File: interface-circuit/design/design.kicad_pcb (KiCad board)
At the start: 2 copper layers, 23 parts, among them J10 Screw_Terminal_01x02, J11 Conn_01x02_Male, J12 Conn_01x02_Male, J2 Screw_Terminal_01x05, J3 Screw_Terminal_01x05, J4 Screw_Terminal_01x02, J5 Conn_01x02_Male, J6 Conn_01x02_Male, J7 Conn_01x03_Male, J8 Conn_01x03_Male, J9 Screw_Terminal_01x02, Q1 2N3904-AP, Q2 2N3904-AP, Q3 2N3904-AP, U1 LogicLevelConverter_BOB-08745

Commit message: WIP
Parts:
- U1: footprint custom-footprints:LOGIC_LEVEL_CONVERTER_BOB11978_BOB8745_XC4486 -> custom-footprints:LOGIC_LEVEL_CONVERTER_BOB-8745
- moved J4 109.6 mm to (127.0, 151.1), turned to 0 degrees
- moved J12 99.4 mm to (112.0, 128.5), turned to 0 degrees
- moved J6 96.6 mm to (138.4, 108.0)
- moved J10 94.9 mm to (138.4, 85.1), turned to 90 degrees
- moved J2 92.4 mm to (138.4, 127.0), turned to 90 degrees
- moved J5 89.9 mm to (34.3, 127.0), turned to 0 degrees
- moved Q3 81.0 mm to (114.3, 80.0), turned to 270 degrees
- moved A1 80.5 mm to (57.4, 119.4)
- moved J3 77.8 mm to (43.2, 149.9), turned to 0 degrees
- moved J9 75.7 mm to (138.4, 97.8), turned to 90 degrees
- moved D1 69.4 mm to (129.5, 108.0)
- moved Q2 67.1 mm to (114.3, 92.7), turned to 270 degrees
- moved D2 66.3 mm to (129.5, 97.8)
- moved Q1 65.2 mm to (114.3, 102.9)
- moved R2 63.2 mm to (109.2, 105.4)
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
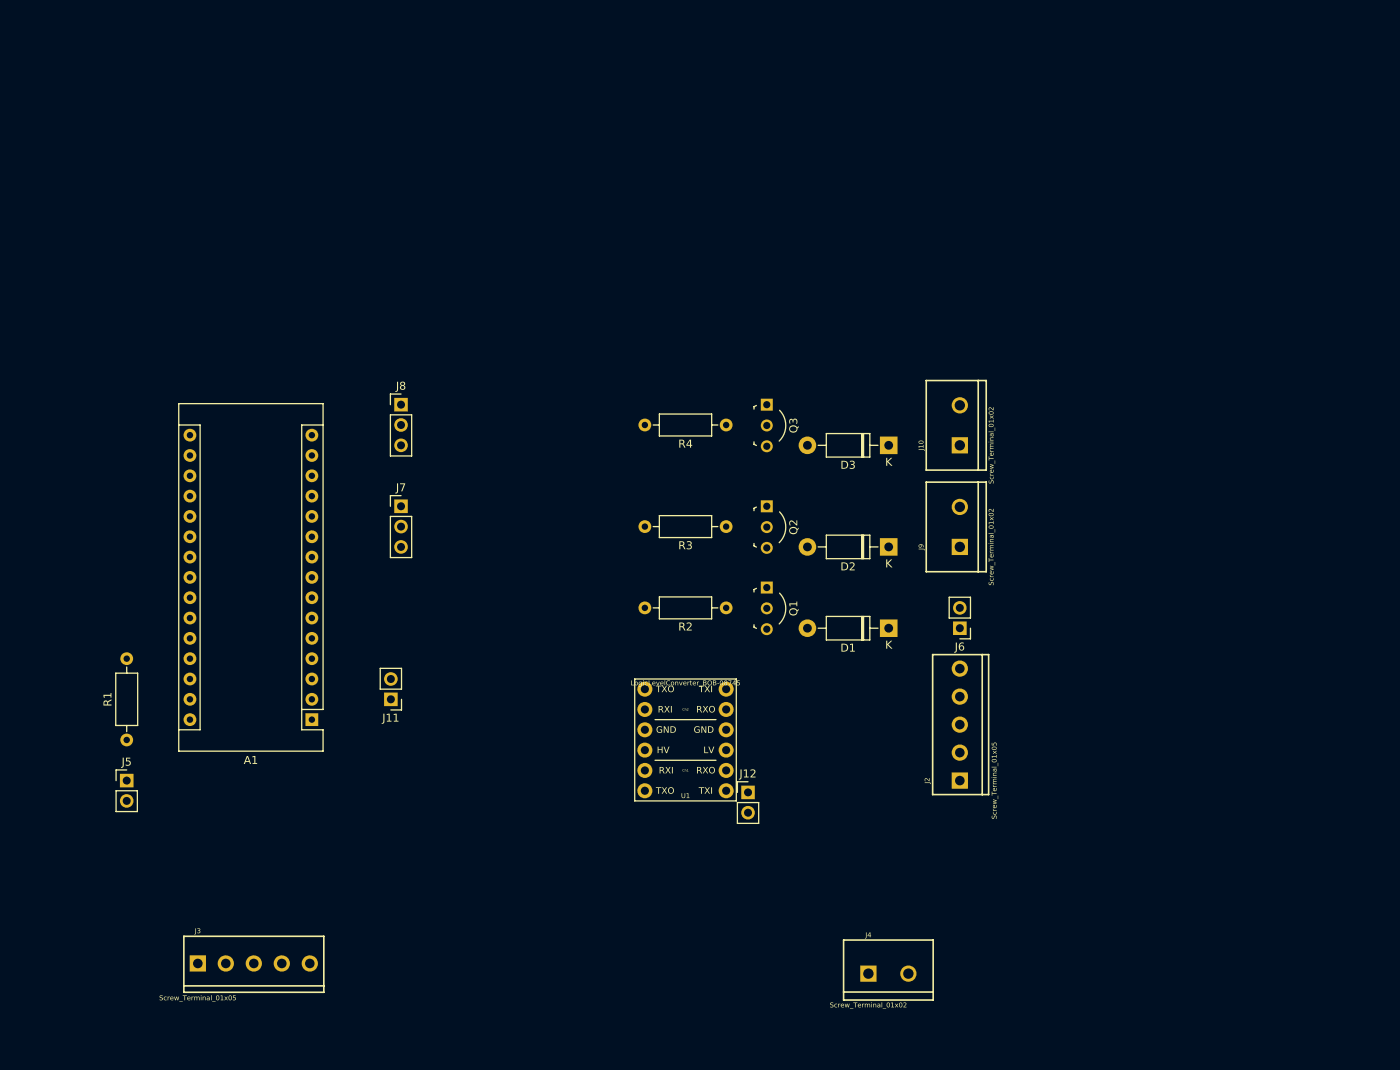
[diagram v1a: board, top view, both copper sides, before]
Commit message: Cannot get the custom component to work, flipped in pcb new and labels associated with wrong sides
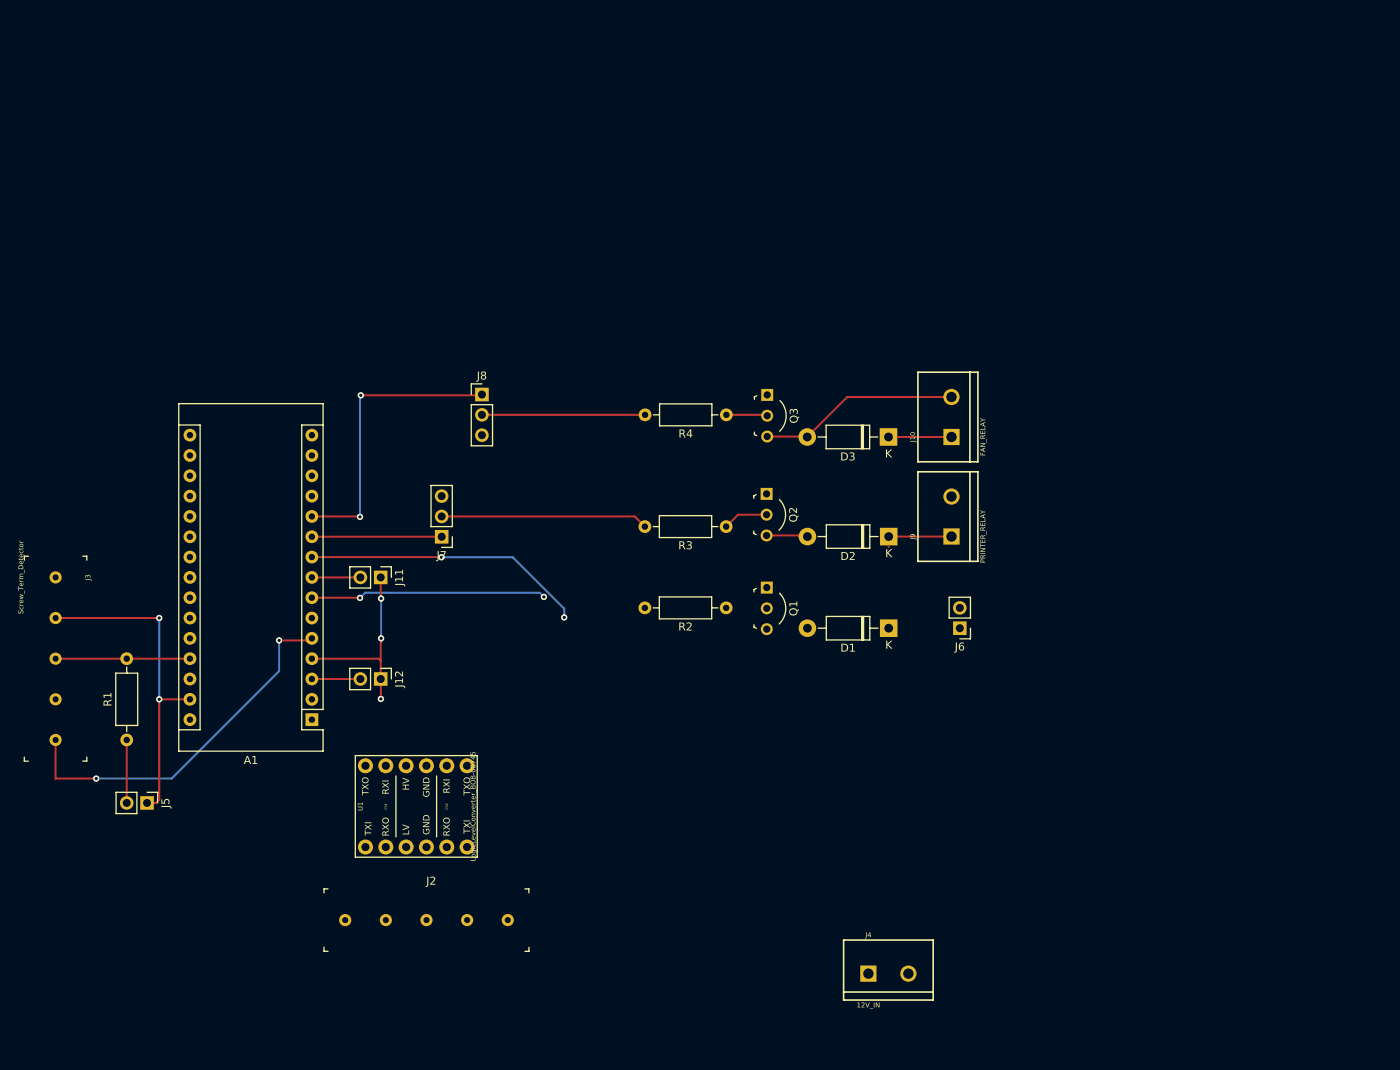
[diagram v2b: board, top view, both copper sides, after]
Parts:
- J10: value Screw_Terminal_01x02 -> FAN_RELAY
- J11: value Conn_01x02_Male -> Conn_Switch
- J12: value Conn_01x02_Male -> Conn_Reset
- J2: value Screw_Terminal_01x05 -> Screw_Term_RPi; footprint Connectors:SCREWTERMINAL-3.5MM-5 -> digikey-footprints:Term_Block_1x5_P5.08mm
- J3: value Screw_Terminal_01x05 -> Screw_Term_Detector; footprint Connectors:SCREWTERMINAL-3.5MM-5 -> digikey-footprints:Term_Block_1x5_P5.08mm
- J4: value Screw_Terminal_01x02 -> 12V_IN
- J5: value Conn_01x02_Male -> Conn_Pwr_LED
- J6: value Conn_01x02_Male -> Conn_Piezo
- J7: value Conn_01x03_Male -> Conn_Printer_Mode
- J8: value Conn_01x03_Male -> Conn_Fan_Mode
- J9: value Screw_Terminal_01x02 -> PRINTER_RELAY
- moved J2 78.8 mm to (61.6, 144.4), turned to 0 degrees
- moved J3 51.4 mm to (25.4, 101.6), turned to 270 degrees
- moved J12 48.1 mm to (66.0, 114.3), turned to 270 degrees
- moved U1 34.7 mm to (70.5, 130.2), turned to 90 degrees
- moved J11 15.3 mm to (66.0, 101.6), turned to 270 degrees
- moved J8 10.2 mm to (78.7, 78.7)
- moved J7 6.35 mm to (73.7, 96.5), turned to 180 degrees
- moved J5 3.78 mm to (36.8, 129.8), turned to 270 degrees
- moved J9 1.66 mm to (137.4, 96.5)
- moved Q2 1.55 mm to (114.3, 91.2)
- moved J10 1.47 mm to (137.4, 84.0)
- moved D2 1.30 mm to (129.5, 96.5)
- moved R4 1.27 mm to (109.2, 81.3)
- moved Q3 1.22 mm to (114.4, 78.8)
- moved D3 1.04 mm to (129.5, 84.0)
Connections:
- A1 pad 29: Net-(A1-Pad29) -> GND
- J2 pad 1: /LV_FanPowerDemand -> /LV_PrinterPowerStatus
- J2 pad 4: /LV_AlarmTriggered -> /LV_FanPowerDemand
- J2 pad 5: /LV_PrinterPowerStatus -> /LV_AlarmTriggered
- U1 pad 1: /HV_PrinterPowerStatus -> /LV_FanPowerDemand
- U1 pad 10: /LV_AlarmTriggered -> /HV_FanPowerDemand
- U1 pad 11: /LV_PrinterPowerDemand -> /LV_PrinterPowerStatus
- U1 pad 12: /LV_FanPowerDemand -> /LV_AlarmTriggered
- U1 pad 2: /HV_AlarmTriggered -> /LV_FanPowerDemand
- U1 pad 3: /HV_PrinterPowerDemand -> /HV_PrinterPowerStatus
- U1 pad 4: /HV_FanPowerDemand -> /HV_AlarmTriggered
- U1 pad 9: /LV_PrinterPowerStatus -> /HV_PrinterPowerDemand
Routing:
- net GND: track 0.00 -> 65.5 mm, vias 0 -> 5
- net /DETECTOR_SIGNAL: track 0.00 -> 46.4 mm, vias 0 -> 2
- net /D8_FAN_RELAY: track 0.00 -> 36.4 mm, vias 0 -> 2
- net /HV_AlarmTriggered: track 0.00 -> 35.3 mm, vias 0 -> 2
- net /HV_FanPowerDemand: track 0.00 -> 29.5 mm, vias 0 -> 2
- net /HV_PrinterPowerStatus: track 0.00 -> 25.9 mm
- net Net-(D3-Pad2): track 0.00 -> 25.1 mm
- net /SW_FAN_RELAY: track 0.00 -> 20.4 mm
- net +5V: track 0.00 -> 16.8 mm
- net /D7_PRINTER_RELAY: track 0.00 -> 16.2 mm
- net +12V: track 0.00 -> 15.8 mm
- net Net-(J5-Pad2): track 0.00 -> 7.87 mm
- net /SOFT_SWITCH: track 0.00 -> 6.06 mm
- net /RESET: track 0.00 -> 6.06 mm
- net Net-(Q2-Pad2): track 0.00 -> 5.67 mm
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
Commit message: Done with manual routing
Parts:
- moved J3 123.5 mm to (146.8, 124.5)
- moved J4 46.4 mm to (147.3, 109.4), turned to 90 degrees
- moved J12 29.0 mm to (43.2, 132.2), turned to 90 degrees
- moved J2 17.6 mm to (73.7, 157.3)
- moved U1 15.2 mm to (82.6, 139.4)
- moved D1 10.3 mm to (139.8, 109.2)
- moved D2 10.2 mm to (139.7, 96.5)
- moved J9 10.2 mm to (147.5, 96.5)
- moved J10 9.94 mm to (147.3, 83.7)
- moved R4 7.98 mm to (116.8, 78.8)
- moved D3 7.65 mm to (137.2, 83.8)
- moved Q3 5.11 mm to (114.3, 83.9), turned to 0 degrees
- moved J7 5.03 mm to (78.7, 96.5), turned to 90 degrees
- moved J6 4.01 mm to (137.2, 104.1), turned to 90 degrees
- moved R3 1.24 mm to (109.2, 94.0)
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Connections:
- J2 pad 1: /LV_PrinterPowerStatus -> /LV_PrinterPowerDemand
- J2 pad 2: /LV_PrinterPowerDemand -> /LV_PrinterPowerStatus
- J2 pad 4: /LV_FanPowerDemand -> /LV_AlarmTriggered
- J2 pad 5: /LV_AlarmTriggered -> /LV_FanPowerDemand
- J7 pad 2: /HV_PrinterPowerStatus -> +5V
- J7 pad 3: +5V -> /HV_PrinterPowerStatus
- J8 pad 2: /SW_FAN_RELAY -> +5V
- J8 pad 3: +5V -> /SW_FAN_RELAY
- U1 pad 1: /LV_FanPowerDemand -> /HV_PrinterPowerStatus
- U1 pad 10: /HV_FanPowerDemand -> /LV_AlarmTriggered
- U1 pad 11: /LV_PrinterPowerStatus -> /HV_PrinterPowerDemand
- U1 pad 12: /LV_AlarmTriggered -> /HV_FanPowerDemand
- U1 pad 2: /LV_FanPowerDemand -> /HV_AlarmTriggered
- U1 pad 3: /HV_PrinterPowerStatus -> /LV_PrinterPowerDemand
- U1 pad 4: /HV_AlarmTriggered -> /LV_FanPowerDemand
- U1 pad 9: /HV_PrinterPowerDemand -> /LV_PrinterPowerStatus
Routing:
- net GND: track 65.5 -> 285.1 mm, vias 5 -> 6
- net +5V: track 16.8 -> 194.1 mm, vias 0 -> 6
- net +3V3: track 0.00 -> 124.6 mm
- net /DETECTOR_SIGNAL: track 46.4 -> 130.6 mm, vias 2 -> 4
- net +12V: track 15.8 -> 73.6 mm
- net /HV_PrinterPowerDemand: track 0.00 -> 46.3 mm, vias 0 -> 3
- net /HV_AlarmTriggered: track 35.3 -> 78.4 mm, vias 2 -> 4
- net /HV_FanPowerDemand: track 29.5 -> 65.0 mm, vias 2 -> 4
- net Net-(D2-Pad2): track 5.16 -> 38.7 mm, vias 0 -> 2
- net /HV_PrinterPowerStatus: track 25.9 -> 59.1 mm, vias 0 -> 3
- net /-PIEZO: track 0.00 -> 25.0 mm
- net /RESET: track 6.06 -> 29.5 mm, vias 0 -> 2
- net /LV_FanPowerDemand: track 0.00 -> 17.7 mm
- net /LV_PrinterPowerDemand: track 0.00 -> 13.9 mm
- net /LV_AlarmTriggered: track 0.00 -> 13.9 mm
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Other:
- board outline added: 126.8 x 83.8 mm
